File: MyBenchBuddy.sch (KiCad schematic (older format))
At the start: 0 parts

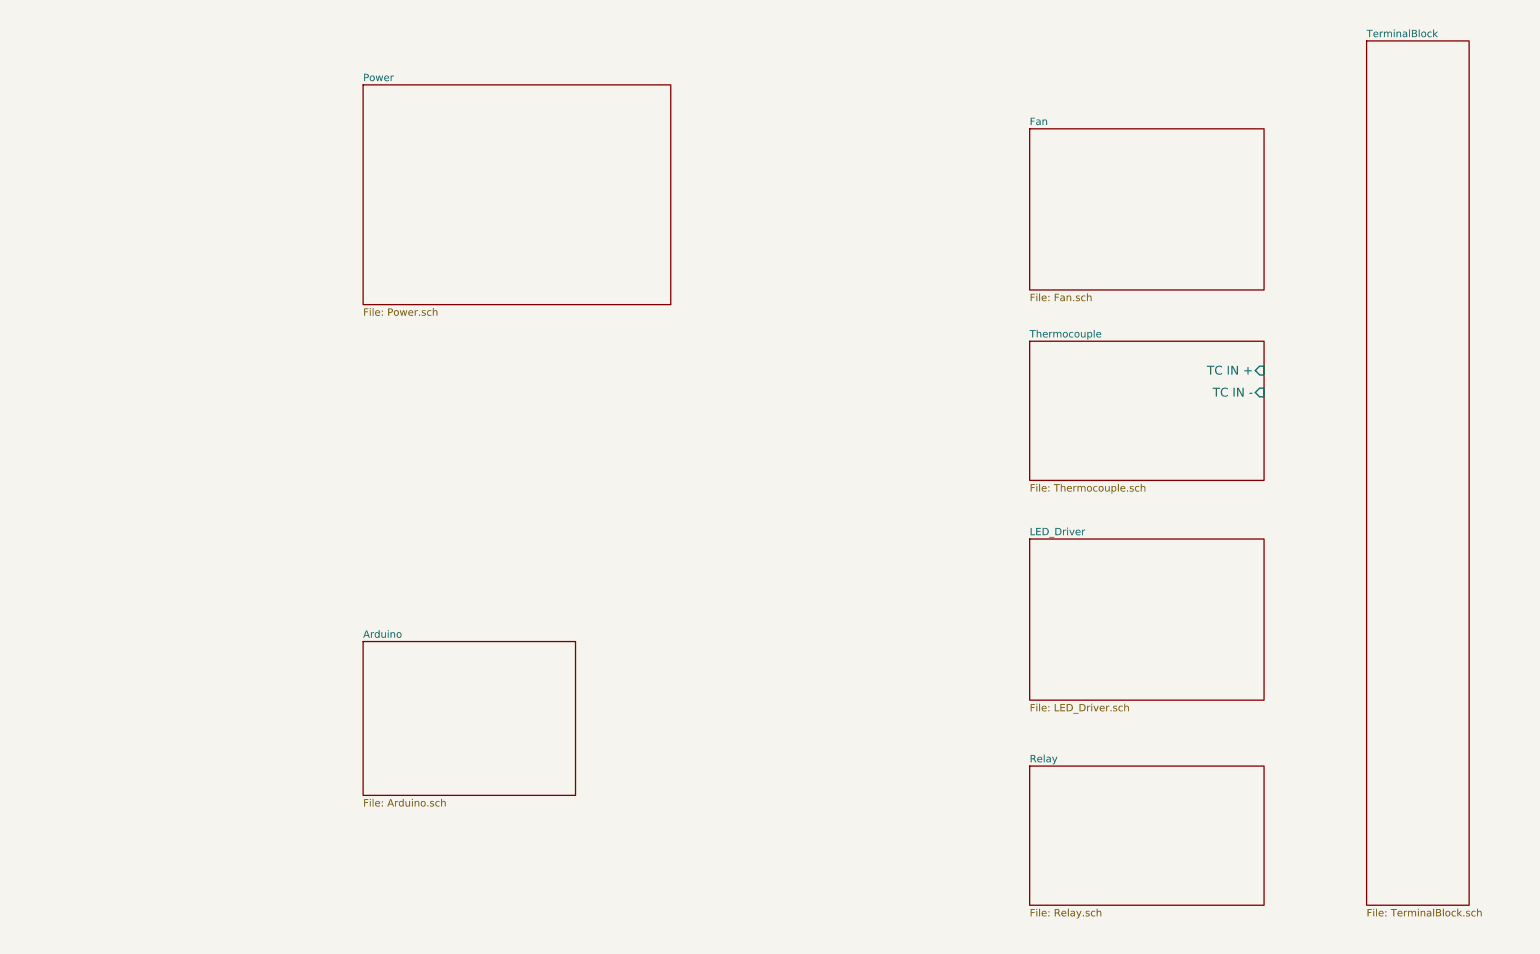
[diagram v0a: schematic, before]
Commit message: Defining Inputs and Outputs
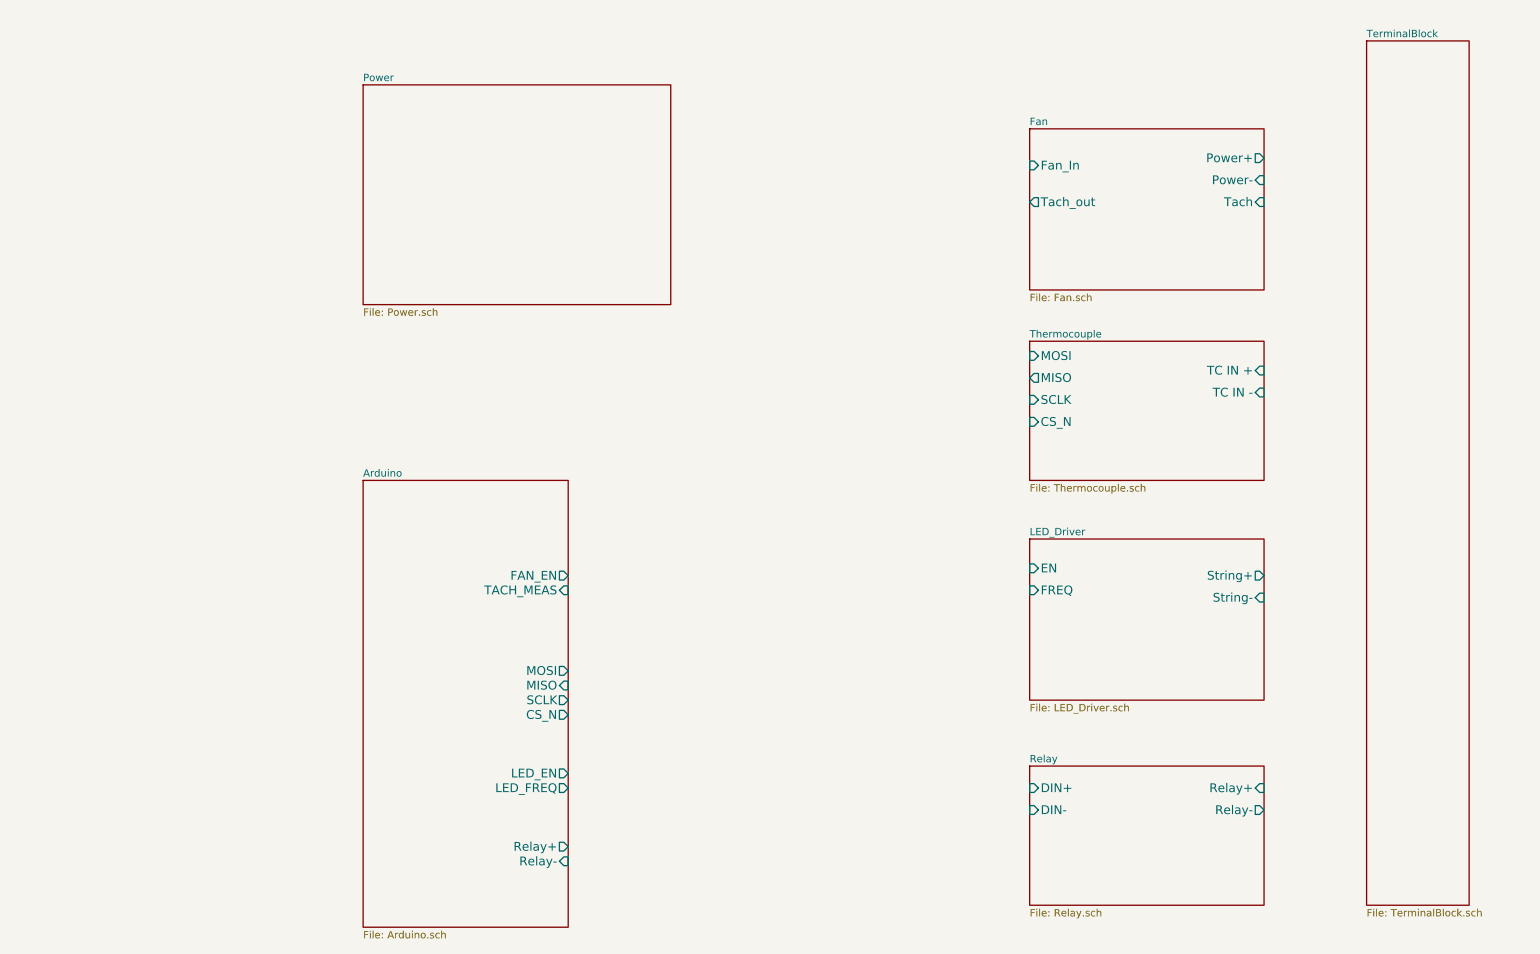
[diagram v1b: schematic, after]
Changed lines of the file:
@@
 $EndDescr
 $Sheet
-S 3350 5000 1450 1050
+S 3350 3900 1400 3050
 U 52340B21
 F0 "Arduino" 50
 F1 "Arduino.sch" 50
+F2 "Relay+" O R 4750 6400 60
+F3 "Relay-" I R 4750 6500 60
+F4 "MOSI" O R 4750 5200 60
+F5 "MISO" I R 4750 5300 60
+F6 "SCLK" O R 4750 5400 60
+F7 "CS_N" O R 4750 5500 60
+F8 "LED_EN" O R 4750 5900 60
+F9 "LED_FREQ" O R 4750 6000 60
+F10 "FAN_EN" O R 4750 4550 60
+F11 "TACH_MEAS" I R 4750 4650 60
 $EndSheet
 $Sheet
@@
 F2 "TC IN +" I R 9500 3150 60
 F3 "TC IN -" I R 9500 3300 60
+F4 "MOSI" I L 7900 3050 60
+F5 "MISO" O L 7900 3200 60
+F6 "SCLK" I L 7900 3350 60
+F7 "CS_N" I L 7900 3500 60
 $EndSheet
 $Sheet
@@
 F0 "Relay" 50
 F1 "Relay.sch" 50
+F2 "DIN+" I L 7900 6000 60
+F3 "DIN-" I L 7900 6150 60
+F4 "Relay+" I R 9500 6000 60
+F5 "Relay-" O R 9500 6150 60
 $EndSheet
 $Sheet
@@
 F0 "LED_Driver" 50
 F1 "LED_Driver.sch" 50
+F2 "EN" I L 7900 4500 60
+F3 "FREQ" I L 7900 4650 60
+F4 "String+" O R 9500 4550 60
+F5 "String-" I R 9500 4700 60
 $EndSheet
 $Sheet
@@
 F0 "Fan" 50
 F1 "Fan.sch" 50
+F2 "Power+" O R 9500 1700 60
+F3 "Power-" I R 9500 1850 60
+F4 "Tach" I R 9500 2000 60
+F5 "Tach_out" O L 7900 2000 60
+F6 "Fan_In" I L 7900 1750 60
 $EndSheet
 $Sheet

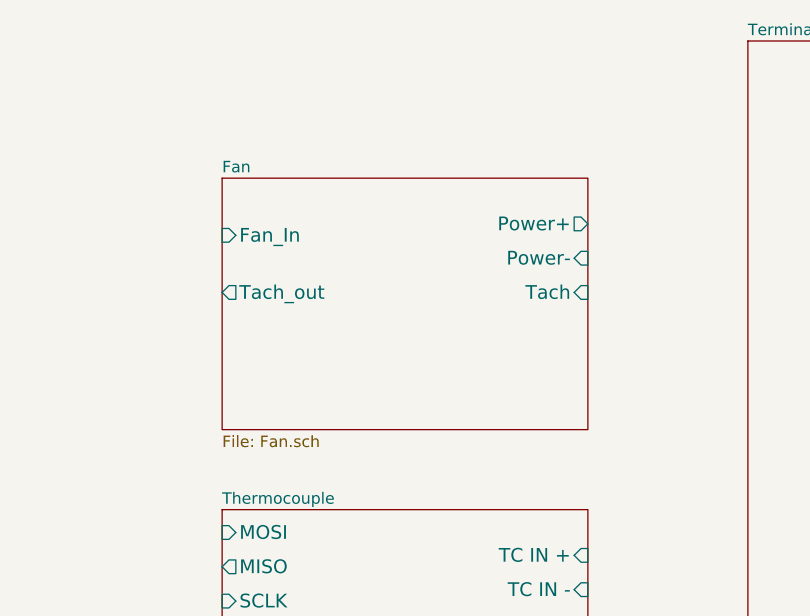
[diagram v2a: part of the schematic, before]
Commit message: Added Fan/Current driver block diagram
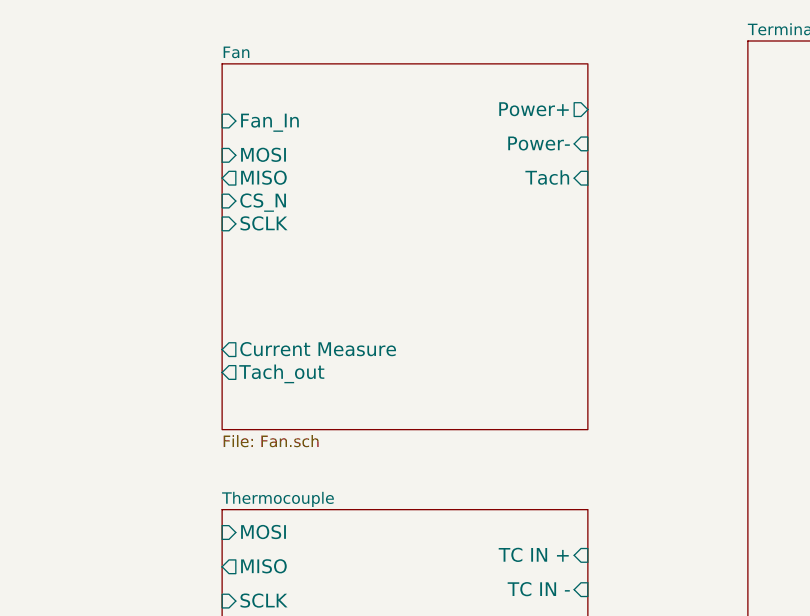
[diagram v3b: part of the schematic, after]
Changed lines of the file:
@@
 $EndSheet
 $Sheet
-S 7900 1500 1600 1100
+S 7900 1000 1600 1600
 U 52340C05
 F0 "Fan" 50
 F1 "Fan.sch" 50
-F2 "Power+" O R 9500 1700 60
-F3 "Power-" I R 9500 1850 60
-F4 "Tach" I R 9500 2000 60
-F5 "Tach_out" O L 7900 2000 60
-F6 "Fan_In" I L 7900 1750 60
+F2 "Power+" O R 9500 1200 60
+F3 "Power-" I R 9500 1350 60
+F4 "Tach" I R 9500 1500 60
+F5 "Tach_out" O L 7900 2350 60
+F6 "Fan_In" I L 7900 1250 60
+F7 "Current Measure" O L 7900 2250 60
+F8 "MOSI" I L 7900 1400 60
+F9 "MISO" O L 7900 1500 60
+F10 "CS_N" I L 7900 1600 60
+F11 "SCLK" I L 7900 1700 60
 $EndSheet
 $Sheet

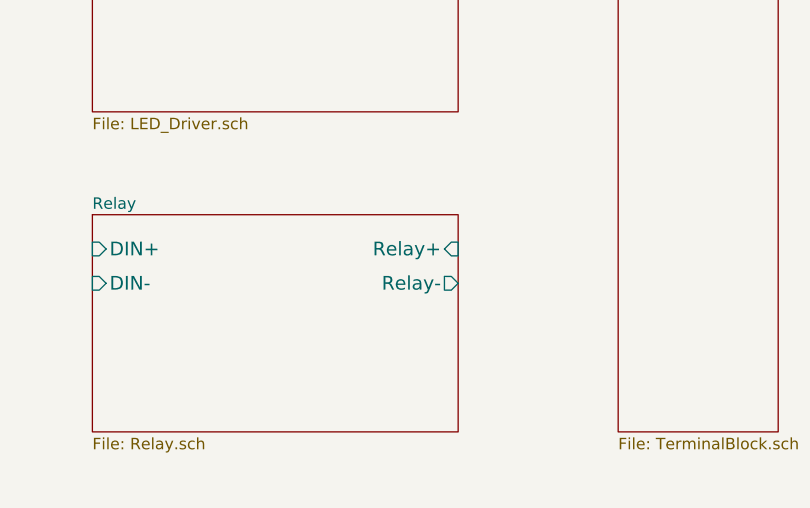
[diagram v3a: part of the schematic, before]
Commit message: Added Relay Module Schematic
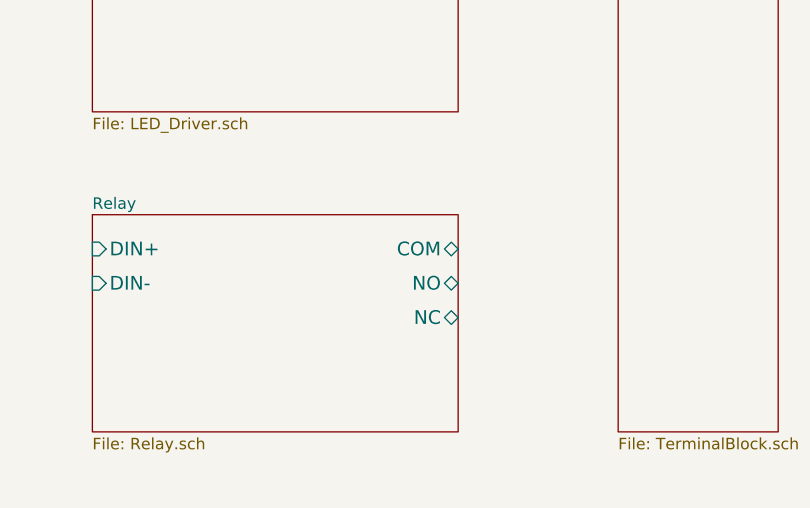
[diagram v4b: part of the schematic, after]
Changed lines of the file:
@@
 LIBS:contrib
 LIBS:valves
+LIBS:BenchBuddy
 LIBS:MyBenchBuddy-cache
 EELAYER 27 0
@@
 Sheet 1 8
 Title ""
-Date "17 sep 2013"
+Date "23 sep 2013"
 Rev ""
 Comp ""
@@
 F2 "DIN+" I L 7900 6000 60
 F3 "DIN-" I L 7900 6150 60
-F4 "Relay+" I R 9500 6000 60
-F5 "Relay-" O R 9500 6150 60
+F4 "NC" B R 9500 6300 60
+F5 "NO" B R 9500 6150 60
+F6 "COM" B R 9500 6000 60
 $EndSheet
 $Sheet

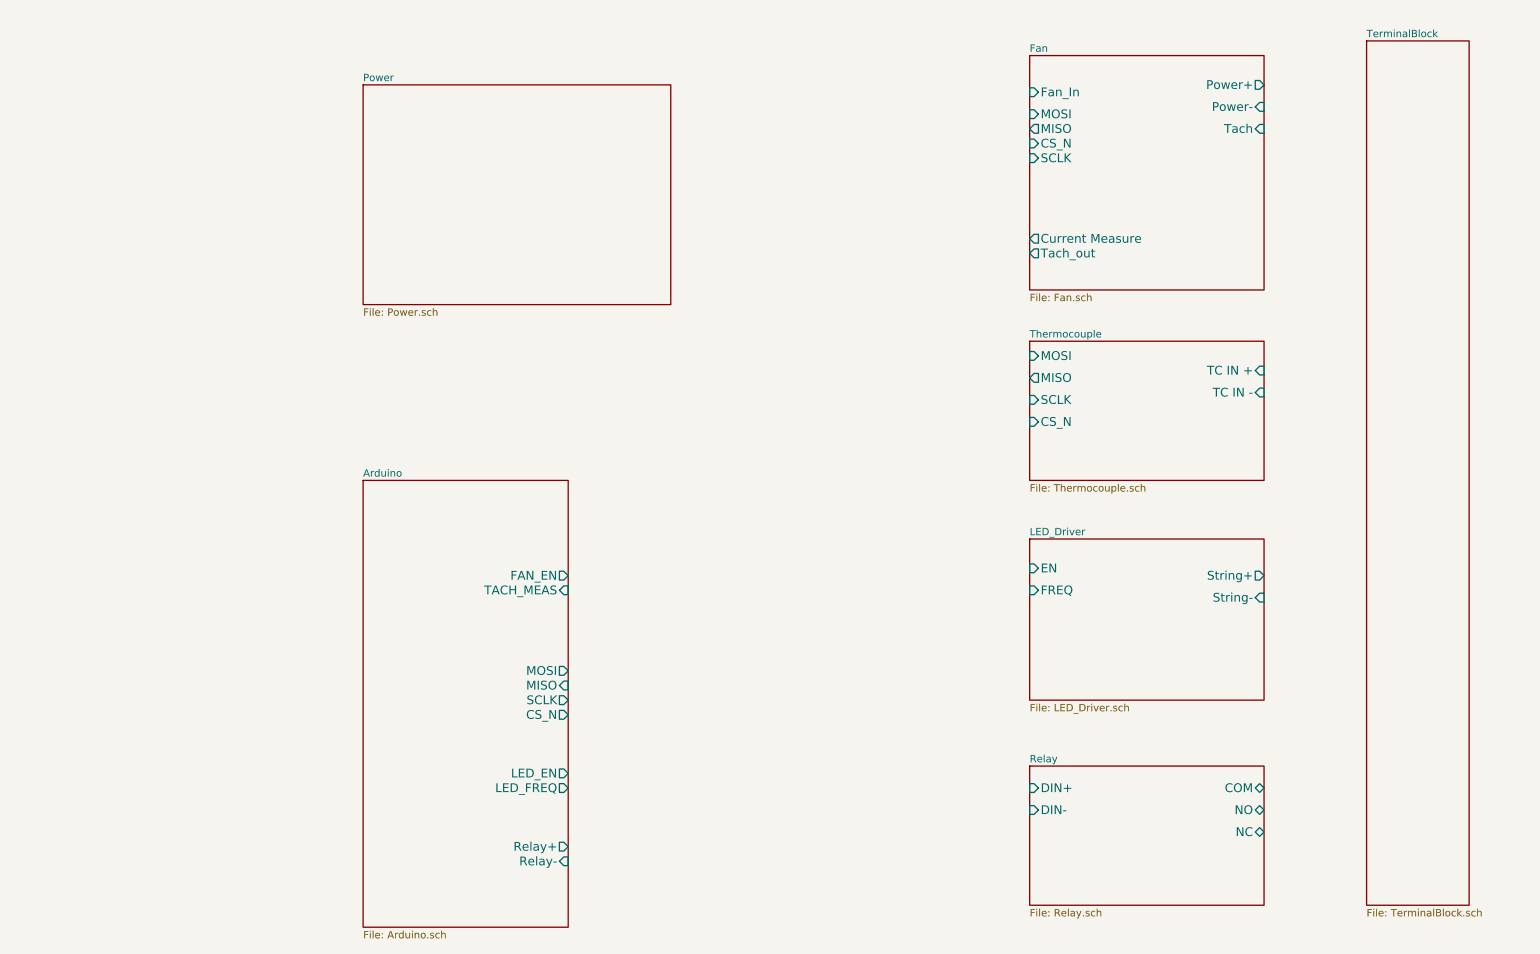
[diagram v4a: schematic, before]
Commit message: Added Power Protection And Filtering Schematic
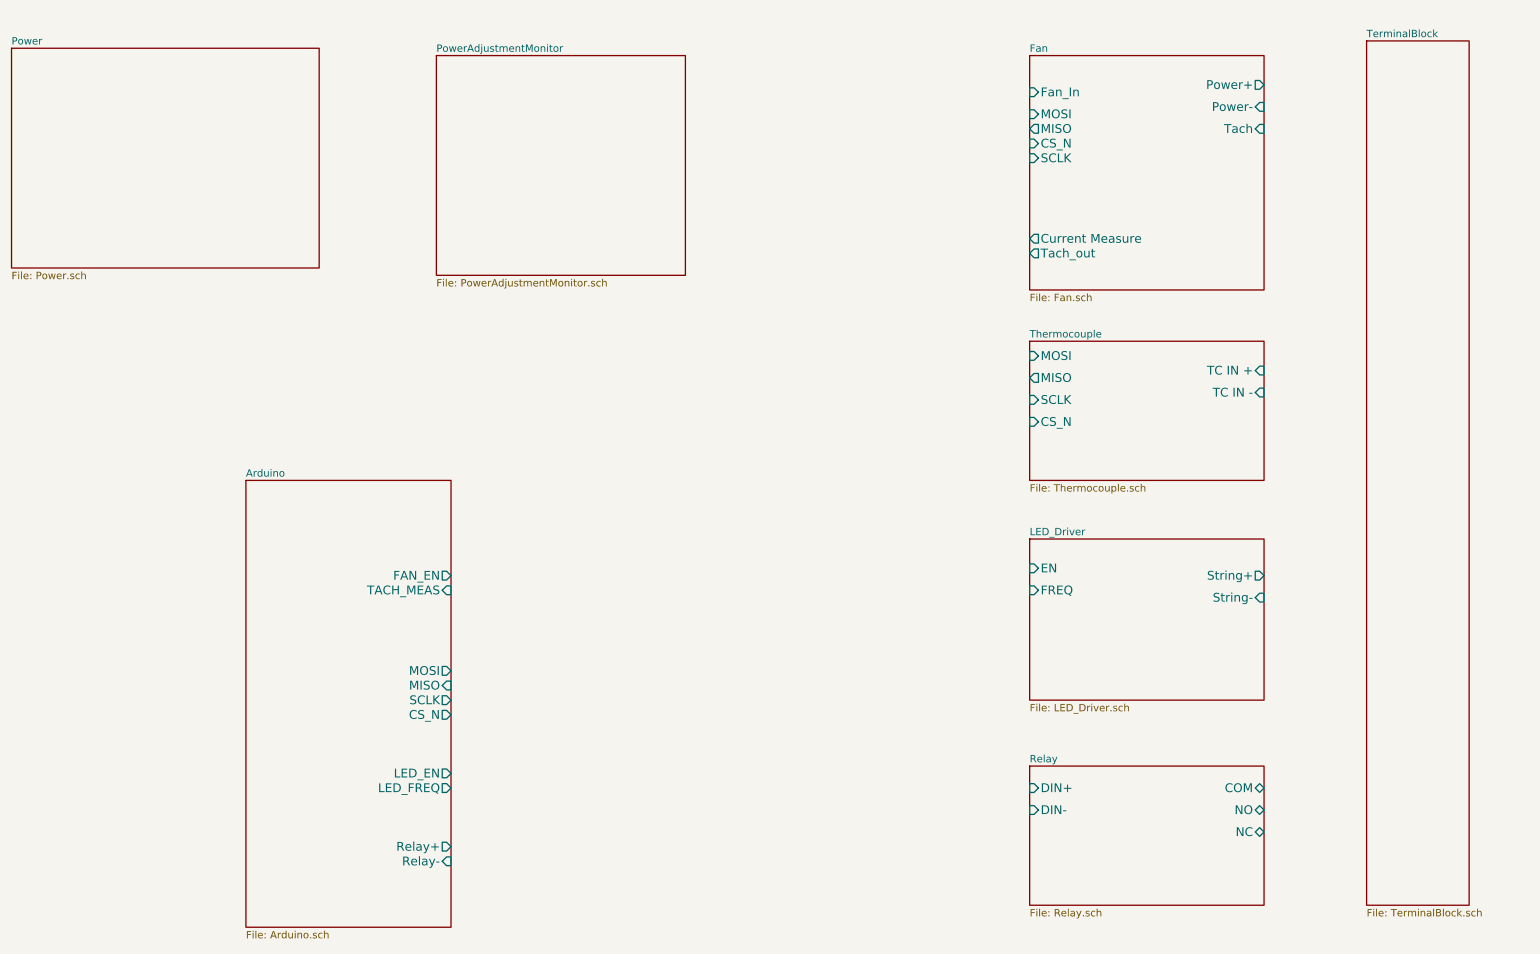
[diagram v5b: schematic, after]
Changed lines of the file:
@@
 $Descr A4 11693 8268
 encoding utf-8
-Sheet 1 8
+Sheet 1 9
 Title ""
 Date "23 sep 2013"
@@
 $EndDescr
 $Sheet
-S 3350 3900 1400 3050
+S 2550 3900 1400 3050
 U 52340B21
 F0 "Arduino" 50
 F1 "Arduino.sch" 50
-F2 "Relay+" O R 4750 6400 60
-F3 "Relay-" I R 4750 6500 60
-F4 "MOSI" O R 4750 5200 60
-F5 "MISO" I R 4750 5300 60
-F6 "SCLK" O R 4750 5400 60
-F7 "CS_N" O R 4750 5500 60
-F8 "LED_EN" O R 4750 5900 60
-F9 "LED_FREQ" O R 4750 6000 60
-F10 "FAN_EN" O R 4750 4550 60
-F11 "TACH_MEAS" I R 4750 4650 60
+F2 "Relay+" O R 3950 6400 60
+F3 "Relay-" I R 3950 6500 60
+F4 "MOSI" O R 3950 5200 60
+F5 "MISO" I R 3950 5300 60
+F6 "SCLK" O R 3950 5400 60
+F7 "CS_N" O R 3950 5500 60
+F8 "LED_EN" O R 3950 5900 60
+F9 "LED_FREQ" O R 3950 6000 60
+F10 "FAN_EN" O R 3950 4550 60
+F11 "TACH_MEAS" I R 3950 4650 60
 $EndSheet
 $Sheet
@@
 $EndSheet
 $Sheet
-S 3350 1200 2100 1500
+S 950  950  2100 1500
 U 52340BB7
 F0 "Power" 50
@@
 F1 "TerminalBlock.sch" 50
 $EndSheet
+$Sheet
+S 3850 1000 1700 1500
+U 523F9073
+F0 "PowerAdjustmentMonitor" 50
+F1 "PowerAdjustmentMonitor.sch" 50
+$EndSheet
 $EndSCHEMATC
